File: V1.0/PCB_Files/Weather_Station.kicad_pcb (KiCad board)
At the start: 2 copper layers, 36 parts, among them J1 Conn_01x04_Socket, J2 USB_B_Micro, J3 Conn_01x04_Pin, J4 Conn_01x04_Pin, J5 Conn_01x06_Pin, U1 STM32F103C8T6, U2 HDC1080DMBR, U3 AMS1117-3.3, U5 SRV05-4, Y1 X322516MLB4SI

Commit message: Finished first version of routing.
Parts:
- moved D1 3.30 mm to (149.9, 76.5)
- moved D3 3.05 mm to (150.0, 73.4)
- moved R8 3.05 mm to (153.1, 73.4), turned to 180 degrees
- moved R6 1.75 mm to (153.1, 75.0), turned to 180 degrees
- moved R7 1.65 mm to (153.1, 76.5), turned to 180 degrees
- moved U5 0.35 mm to (179.1, 79.1)
- moved D2 0.11 mm to (150.0, 75.0)
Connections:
- U1 pad 10: /LED_B -> unconnected-(U1-PA0-Pad10)
- U1 pad 11: /LED_W -> unconnected-(U1-PA1-Pad11)
- U1 pad 12: /LED_R -> unconnected-(U1-PA2-Pad12)
- U1 pad 2: unconnected-(U1-PC13-Pad2) -> /LED_B
- U1 pad 3: unconnected-(U1-PC14-Pad3) -> /LED_R
- U1 pad 4: unconnected-(U1-PC15-Pad4) -> /LED_W
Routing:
- net +3.3V: track 7.93 -> 94.3 mm, vias 0 -> 6
- net /I2C1_SCL: track 0.00 -> 46.5 mm, vias 0 -> 1
- net /I2C1_SDA: track 0.00 -> 42.2 mm, vias 0 -> 1
- net VBUS: track 0.00 -> 42.2 mm, vias 0 -> 5
- net /USART1_TX: track 0.00 -> 16.2 mm, vias 0 -> 1
- net /LED_B: track 0.00 -> 14.1 mm, vias 0 -> 2
- net /LED_R: track 0.00 -> 13.8 mm, vias 0 -> 2
- net /LED_W: track 0.00 -> 13.5 mm, vias 0 -> 2
- net /USART1_RX: track 0.00 -> 13.0 mm, vias 0 -> 1
- net /OSC_IN: track 0.00 -> 8.59 mm
- net /USB_D-: track 7.33 -> 15.5 mm
- net /SWCLK: track 0.00 -> 8.16 mm
- net /USB_D+: track 7.45 -> 15.5 mm
- net /SWDIO: track 0.00 -> 6.71 mm
- net /OSC_OUT: track 0.00 -> 6.12 mm
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- added copper zone on F.Cu, net +3.3V
- added copper zone on F.Cu, net /VBUS_IN
- added copper zone on F.Cu, net VBUS

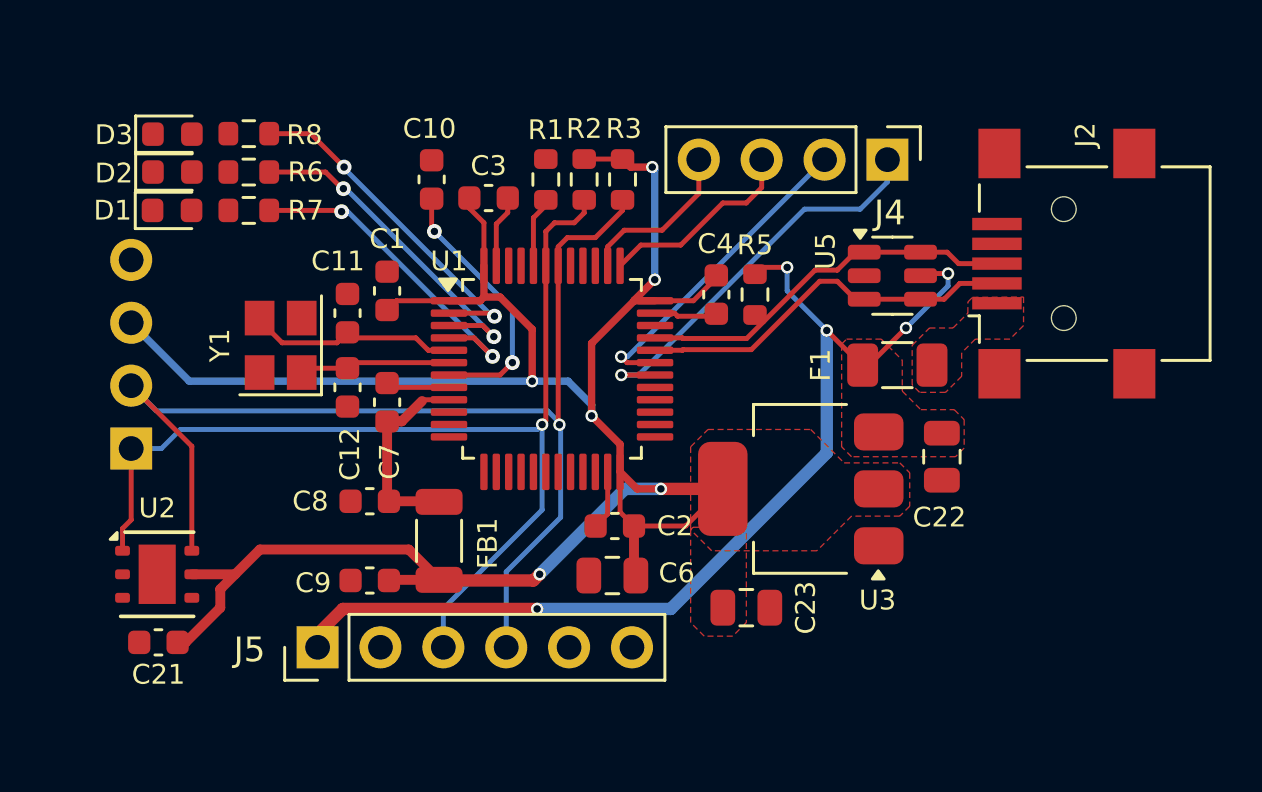
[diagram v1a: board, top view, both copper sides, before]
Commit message: Changed Micro USB to USB.
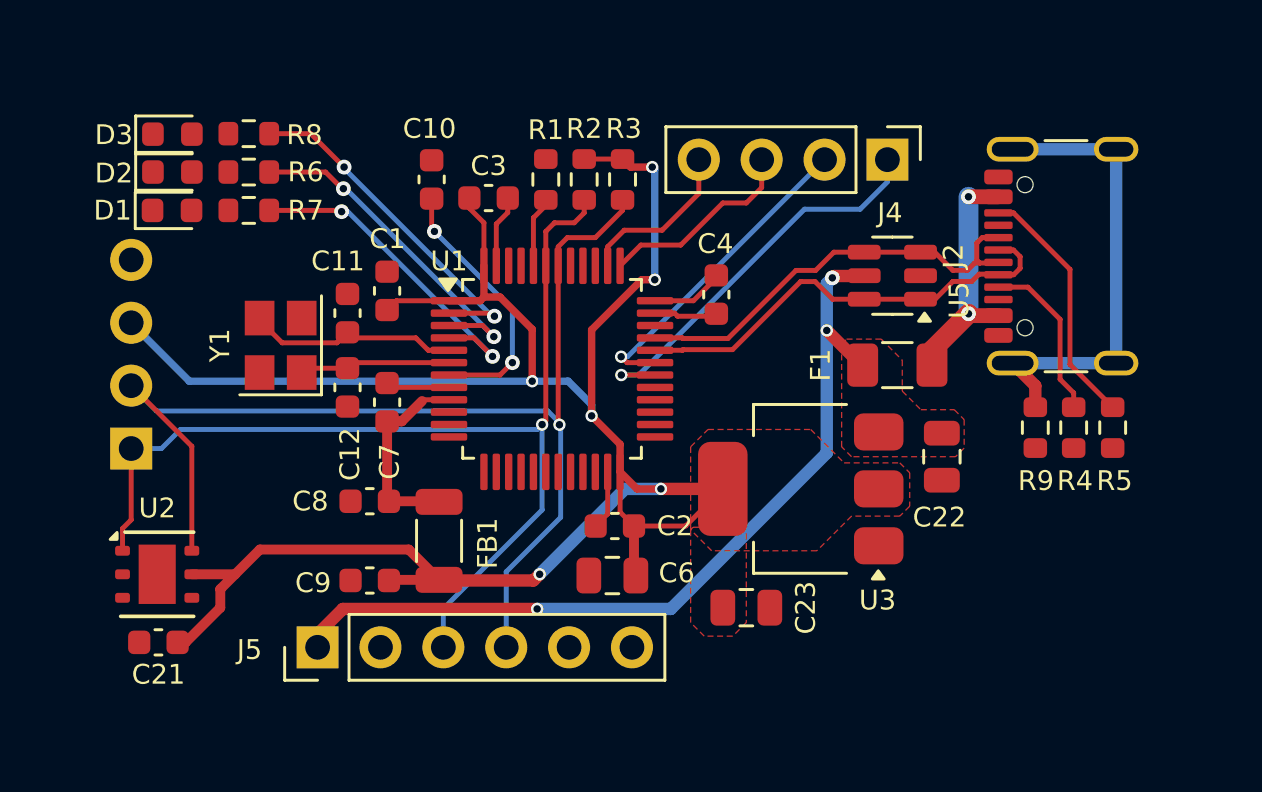
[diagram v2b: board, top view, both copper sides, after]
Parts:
- added R4: 5k1, Resistor_SMD:R_0603_1608Metric, F.Cu at (186.4, 85.3)
- added R9: 1M, Resistor_SMD:R_0603_1608Metric, F.Cu at (184.8, 85.3)
- J2: value USB_B_Micro -> TYPE-C16PIN; footprint Connector_USB:USB_Mini-B_Lumberg_2486_01_Horizontal -> Connector_USB:USB_C_Receptacle_GCT_USB4105-xx-A_16P_TopMnt_Horizontal
- R5: value 1k5 -> 5k1
- moved R5 15.4 mm to (187.9, 85.3)
- moved J2 1.08 mm to (187.0, 78.3)
- turned U5 to 180 degrees
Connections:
- R5 pad 1: VBUS -> /CC2
- R5 pad 2: /USB_D+ -> GND
- U5 pad 1: /USB_D+ -> /USB_D-
- U5 pad 3: /USB_D- -> /USB_D+
- U5 pad 4: /USB_D- -> /USB_D+
- U5 pad 6: /USB_D+ -> /USB_D-
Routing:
- net Net-(J2-SHIELD): track 0.00 -> 19.1 mm
- net /CC2: track 0.00 -> 10.1 mm
- net /VBUS_IN: track 0.00 -> 9.86 mm, vias 0 -> 2
- net VBUS: track 42.2 -> 34.7 mm, vias 5 -> 3
- net /CC1: track 0.00 -> 6.81 mm
- net /USB_D-: track 15.5 -> 18.2 mm
- net /USB_D+: track 15.5 -> 17.6 mm
- net +3.3V: track 94.3 -> 93.8 mm
- removed copper zone on F.Cu, net /VBUS_IN

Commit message: Routing of V1 should be finsihed.
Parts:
- added G***: LOGO, LOGO, B.Cu at (168.8, 73.6)
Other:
- board outline added: 44.7 x 25.5 mm
- board text added: "5V"
- board text added: "CLK"
- board text added: "GND"
- board text added: "INT"
- board text added: "RX"
- board text added: "SCL"
- board text added: "SDA"
- board text added: "SWD"
- board text added: "TX"
- board text added: "Weather Station V1.0"

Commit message: V1.0 should be finished.
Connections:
- U1 pad 18: unconnected-(U1-PB0-Pad18) -> /RTC_CLK
- U1 pad 19: unconnected-(U1-PB1-Pad19) -> /RTC_INT
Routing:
- net GND: track 10.4 -> 50.3 mm, vias 0 -> 59
- net /RTC_INT: track 0.00 -> 8.84 mm
- net /RTC_CLK: track 0.00 -> 7.48 mm
- net Net-(D1-A): track 0.00 -> 1.49 mm
- net Net-(D3-A): track 0.00 -> 1.48 mm
- net Net-(D2-A): track 0.00 -> 1.47 mm
- net /I2C1_SCL: track 46.5 -> 47.4 mm
- net +3.3V: track 94.1 -> 94.5 mm, vias 6 -> 9
- added copper zone on B.Cu, net GND
- added copper zone on F.Cu, net GND
- added copper zone on In1.Cu, net GND
- added copper zone on In2.Cu, net GND
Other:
- board size 44.7 x 25.5 mm -> 44.7 x 26.1 mm
- copper layers 2 -> 4
- board text added: "Debug"
- board text added: "Display"
- board text added: "RTC"
- board text added: "Sensor"

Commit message: DRC is to do but otherwise should be V1.
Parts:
- J1: value Conn_01x04_Socket -> HS91L02W2C01
- J3, J4: value Conn_01x04_Pin -> B-2100S04P-A110
- J5: value Conn_01x06_Pin -> ZX-PZ2.54-1-6PZZ
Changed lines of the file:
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@@
 			)
 		)
-		(property "Value" "Conn_01x04_Pin"
+		(property "Value" "B-2100S04P-A110"
 			(at 0 9.95 -90)
 			(layer "F.Fab")
@@
 			)
 		)
-		(property "Value" "Conn_01x06_Pin"
+		(property "Value" "ZX-PZ2.54-1-6PZZ"
 			(at 0 15.03 90)
 			(layer "F.Fab")
@@
 			)
 		)
-		(property "Value" "Conn_01x04_Socket"
+		(property "Value" "HS91L02W2C01"
 			(at 0 -1.16 0)
 			(layer "B.Fab")
@@
 			)
 		)
-		(property "Description" "Generic connector, single row, 01x04, script generated"
+		(property "Description" "Display"
 			(at 0 0 180)
 			(unlocked yes)
@@
 			)
 		)
-		(property "Value" "Conn_01x04_Pin"
+		(property "Value" "B-2100S04P-A110"
 			(at 0 -9.95 0)
 			(layer "B.Fab")

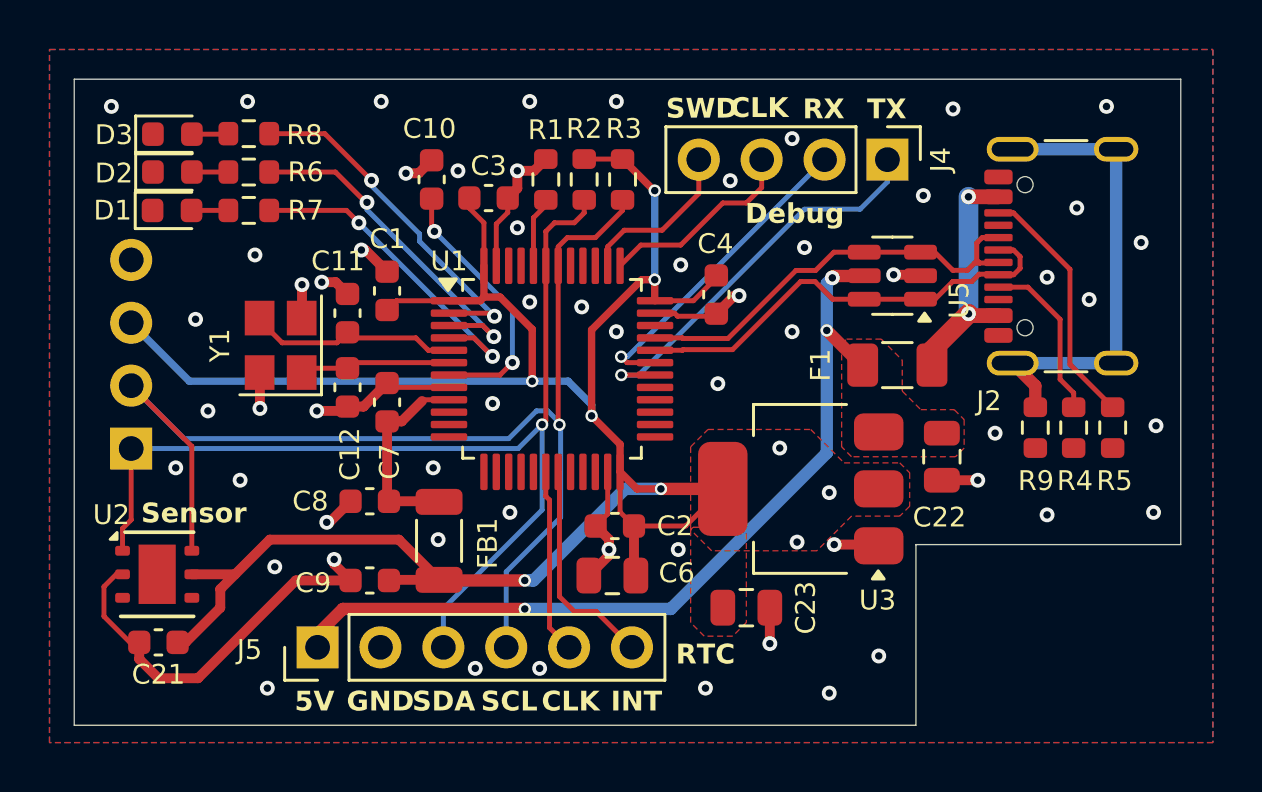
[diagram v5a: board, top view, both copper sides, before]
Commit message: Changed Fuse and added SWD Restistor.
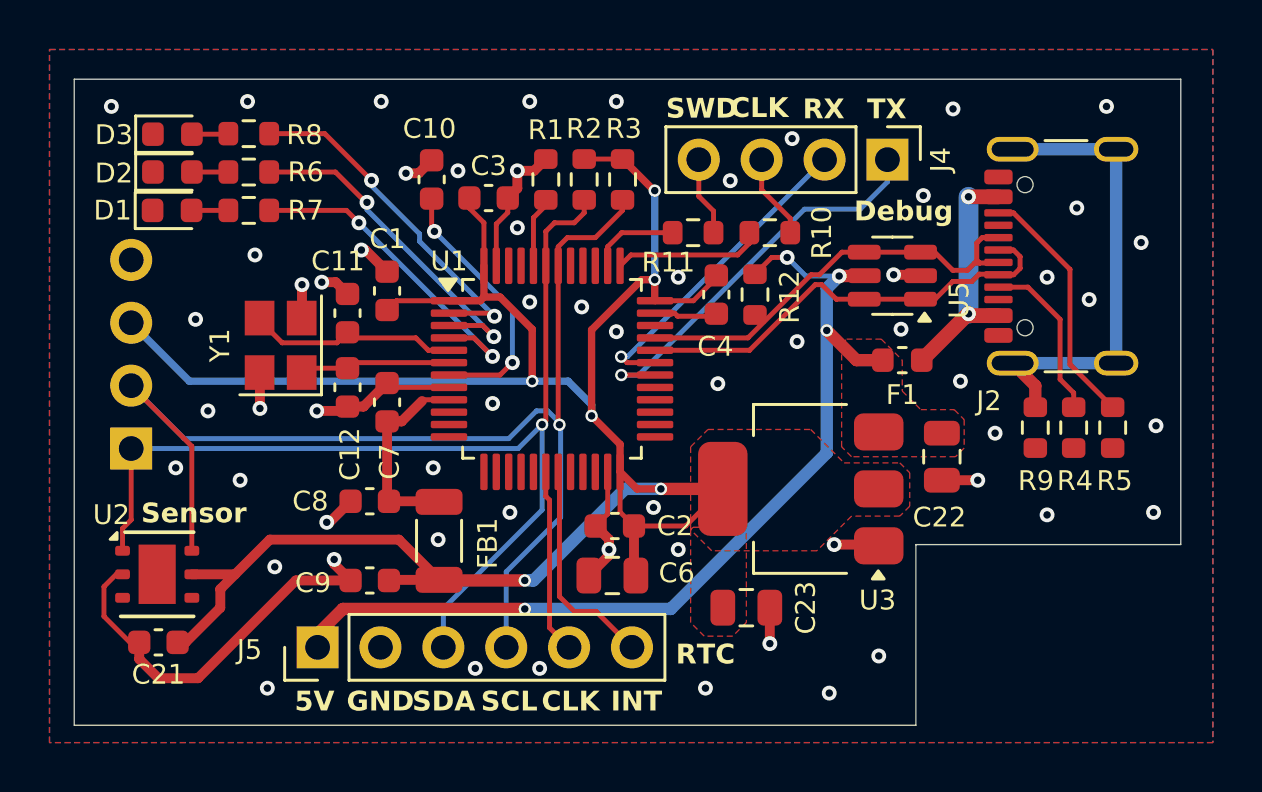
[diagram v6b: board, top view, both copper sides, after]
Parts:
- added R10: 100R, Resistor_SMD:R_0603_1608Metric, F.Cu at (174.1, 77.4)
- added R11: 100R, Resistor_SMD:R_0603_1608Metric, F.Cu at (171.0, 77.4)
- added R12: 1k5, Resistor_SMD:R_0603_1608Metric, F.Cu at (173.5, 79.9)
- F1: value JFC1206-1100FS -> CFS06V3T1R0; footprint Fuse:Fuse_1206_3216Metric -> Fuse:Fuse_0603_1608Metric
- moved F1 0.28 mm to (179.4, 82.5)
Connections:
- U1 pad 37: /SWCLK -> /uC_SWCLK
- U1 pad 38: /SWDIO -> /uC_SWDIO
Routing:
- net /uC_SWCLK: track 0.00 -> 6.03 mm
- net /SWCLK: track 8.16 -> 3.43 mm
- net VBUS: track 34.7 -> 39.3 mm, vias 3 -> 4
- net /uC_SWDIO: track 0.00 -> 3.63 mm
- net /SWDIO: track 6.71 -> 3.20 mm
- net GND: track 50.3 -> 49.0 mm, vias 59 -> 60
- net +3.3V: vias 9 -> 6
